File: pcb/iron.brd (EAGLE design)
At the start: 8 x 48 mm, 22 parts, among them IC1 AT24CS04-SOT23, IC2 TS507CLT, IC3 AD7995, IC4 ESDA6V1SC5, X1 LUMBERG_KLB_4

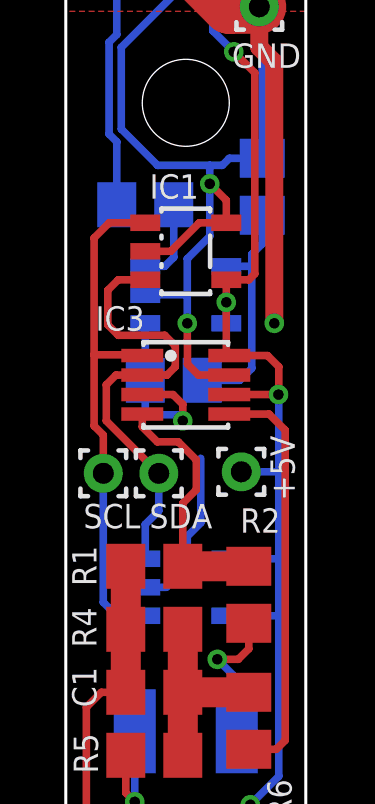
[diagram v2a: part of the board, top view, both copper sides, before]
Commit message: fixing op amp (iron,tweezer)
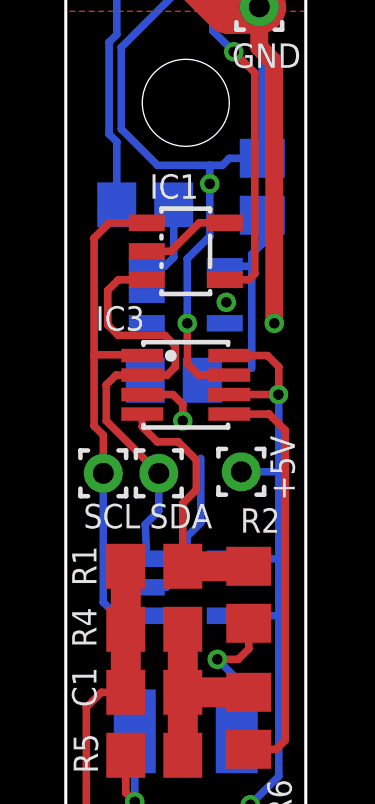
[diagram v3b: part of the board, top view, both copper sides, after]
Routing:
- net AD_TC: track 6.33 -> 2.03 mm
- net +5V: track 57.1 -> 53.9 mm
- net GND: track 60.1 -> 57.0 mm
- net FEEDBACK: track 7.91 -> 6.14 mm
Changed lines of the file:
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@@
 <attribute name="VALUE" x="3.585" y="21.49" size="1.27" layer="27" rot="R180"/>
 </element>
-<element name="R2" library="solderpi" library_urn="urn:adsk.eagle:library:1437534" package="R0805" package3d_urn="urn:adsk.eagle:package:1581953/2" value="68k @25°C, 1%, ß=4100 K" x="6.1" y="18" smashed="yes" rot="R90">
+<element name="R2" library="solderpi" library_urn="urn:adsk.eagle:library:1437534" package="R0805" package3d_urn="urn:adsk.eagle:package:1581953/4" value="68k @25°C, 1%, ß=4100 K" x="6.1" y="18" smashed="yes" rot="R90">
 <attribute name="NAME" x="5.815" y="20.07" size="0.8128" layer="25"/>
 <attribute name="VALUE" x="8.64" y="17.365" size="1.27" layer="27" rot="R90"/>
@@
 <attribute name="VALUE" x="9.09" y="32.235" size="1.27" layer="28" rot="MR270"/>
 </element>
-<element name="IC2" library="solderpi" library_urn="urn:adsk.eagle:library:1437534" package="SOT23-5L" package3d_urn="urn:adsk.eagle:package:1437676/4" value="TS507CLT" x="4" y="28" smashed="yes" rot="MR90">
+<element name="IC2" library="solderpi" library_urn="urn:adsk.eagle:library:1437534" package="SOT23-5L" package3d_urn="urn:adsk.eagle:package:1437676/7" value="TS507CLT" x="4" y="28" smashed="yes" rot="MR90">
 <attribute name="NAME" x="6.105" y="27.495" size="0.8128" layer="26" rot="MR90"/>
 <attribute name="OC_MOUSER" value="511-TS507CLT" x="4" y="28" size="1.778" layer="28" rot="MR90" display="off"/>
@@
 <attribute name="VALUE" x="5.85" y="22.7" size="0.0254" layer="27"/>
 </element>
-<element name="IC1" library="solderpi" library_urn="urn:adsk.eagle:library:1437534" package="SOT23-5L" package3d_urn="urn:adsk.eagle:package:1437676/4" value="AT24CS04-SOT23" x="4" y="29.45" smashed="yes" rot="R270">
+<element name="IC1" library="solderpi" library_urn="urn:adsk.eagle:library:1437534" package="SOT23-5L" package3d_urn="urn:adsk.eagle:package:1437676/7" value="AT24CS04-SOT23" x="4" y="29.45" smashed="yes" rot="R270">
 <attribute name="NAME" x="2.795" y="31.205" size="0.8128" layer="25"/>
 <attribute name="OC_MOUSER" value="556-AT24CS04-STUM-T" x="4" y="29.45" size="1.778" layer="27" rot="R270" display="off"/>
 <attribute name="VALUE" x="0.571" y="31.355" size="1.27" layer="27" rot="R270"/>
 </element>
-<element name="IC4" library="solderpi" library_urn="urn:adsk.eagle:library:1437534" package="SOT23-5L" package3d_urn="urn:adsk.eagle:package:1437676/4" value="ESDA6V1SC5" x="4" y="18.25" smashed="yes" rot="MR90">
+<element name="IC4" library="solderpi" library_urn="urn:adsk.eagle:library:1437534" package="SOT23-5L" package3d_urn="urn:adsk.eagle:package:1437676/7" value="ESDA6V1SC5" x="4" y="18.25" smashed="yes" rot="MR90">
 <attribute name="NAME" x="6.355" y="17.545" size="0.8128" layer="26" rot="MR90"/>
 <attribute name="VALUE" x="0.571" y="16.345" size="1.27" layer="28" rot="MR90"/>
@@
 <wire x1="4" y1="39.05" x2="4" y2="44.15" width="1.8" layer="1"/>
 <wire x1="5.45" y1="37.6" x2="4" y2="39.05" width="1.8" layer="1"/>
-<wire x1="5.35" y1="31.15" x2="4.8" y2="31.7" width="0.254" layer="1"/>
 <via x="4.8" y="31.7" extent="1-16" drill="0.35"/>
 <contactref element="IC1" pad="2"/>
 <contactref element="IC1" pad="5"/>
-<wire x1="5.35" y1="30.4" x2="5.35" y2="31.15" width="0.254" layer="1"/>
-<wire x1="2.65" y1="29.45" x2="3.5" y2="29.45" width="0.254" layer="1"/>
+<wire x1="2.7" y1="29.45" x2="3.5" y2="29.45" width="0.254" layer="1"/>
 <wire x1="3.5" y1="29.45" x2="4.45" y2="30.4" width="0.254" layer="1"/>
-<wire x1="4.45" y1="30.4" x2="5.35" y2="30.4" width="0.254" layer="1"/>
+<wire x1="4.45" y1="30.4" x2="5.3" y2="30.4" width="0.254" layer="1"/>
 <polygon width="0.2" layer="16" isolate="0.3048" rank="2">
 <vertex x="0" y="48"/>
@@
 <wire x1="5.7" y1="13.45" x2="5.7" y2="15.2" width="0.254" layer="16"/>
 <contactref element="IC4" pad="2"/>
-<wire x1="2.65" y1="18.25" x2="3.35" y2="18.25" width="0.254" layer="16"/>
+<wire x1="2.7" y1="18.25" x2="3.35" y2="18.25" width="0.254" layer="16"/>
 <wire x1="3.35" y1="18.25" x2="4.05" y2="18.95" width="0.254" layer="16"/>
 <wire x1="4.05" y1="18.95" x2="4.05" y2="19.95" width="0.254" layer="16"/>
@@
 <wire x1="6.45" y1="36.25" x2="6.45" y2="37.6" width="0.6" layer="1"/>
 <wire x1="6.95" y1="35.75" x2="6.45" y2="36.25" width="0.6" layer="1"/>
-<contactref element="IC2" pad="2"/>
 <wire x1="4.05" y1="27.05" x2="4.05" y2="28" width="0.254" layer="16"/>
 <wire x1="4.05" y1="28" x2="4.05" y2="29.2" width="0.254" layer="16"/>
 <wire x1="4.05" y1="29.2" x2="4.8" y2="29.95" width="0.254" layer="16"/>
-<wire x1="2.65" y1="28" x2="4.05" y2="28" width="0.254" layer="16"/>
+<contactref element="IC2" pad="2"/>
+<wire x1="4.8" y1="29.95" x2="4.45" y2="30.4" width="0" layer="19" extent="1-16"/>
 </signal>
 <signal name="AD_COMP">
@@
 <wire x1="7.1" y1="19.2" x2="7.1" y2="22.1" width="0.254" layer="16"/>
 <wire x1="7.1" y1="22.1" x2="7.1" y2="24.6642" width="0.254" layer="16"/>
-<wire x1="5.35" y1="19.2" x2="7.1" y2="19.2" width="0.254" layer="16"/>
+<wire x1="5.3" y1="19.2" x2="7.1" y2="19.2" width="0.254" layer="16"/>
 <wire x1="7.1" y1="11.95" x2="6.15" y2="11" width="0.254" layer="16"/>
 <via x="6.15" y="11" extent="1-16" drill="0.35"/>
@@
 <wire x1="1.1858" y1="14.75" x2="2" y2="14.75" width="0.254" layer="1"/>
 <wire x1="5.15" y1="10" x2="1.2858" y2="10" width="0.254" layer="1"/>
-<wire x1="5.35" y1="17.3" x2="7.1" y2="17.3" width="0.254" layer="16"/>
+<wire x1="5.3" y1="17.3" x2="7.1" y2="17.3" width="0.254" layer="16"/>
 <wire x1="5.85" y1="22.1" x2="7.1" y2="22.1" width="0.254" layer="16"/>
-<contactref element="IC2" pad="5"/>
-<wire x1="5.35" y1="27.05" x2="5.35" y2="27.75" width="0.254" layer="16"/>
 <via x="5.35" y="27.75" extent="1-16" drill="0.35"/>
-<wire x1="5.35" y1="27.75" x2="5.35" y2="28.5" width="0.254" layer="1"/>
-<wire x1="5.45" y1="25.975" x2="5.35" y2="25.975" width="0.254" layer="1"/>
-<wire x1="5.35" y1="25.975" x2="5.35" y2="27.75" width="0.254" layer="1"/>
-<wire x1="5.35" y1="28.5" x2="6.1" y2="28.5" width="0.254" layer="1"/>
+<wire x1="5.3" y1="28.5" x2="6.1" y2="28.5" width="0.254" layer="1"/>
 <wire x1="6.1" y1="28.5" x2="6.3" y2="28.7" width="0.254" layer="1"/>
 <wire x1="6.3" y1="28.7" x2="6.3" y2="35.4" width="0.254" layer="1"/>
@@
 <wire x1="5.6" y1="36.1" x2="4.9" y2="36.8" width="0.254" layer="16"/>
 <wire x1="4.9" y1="36.8" x2="4.9" y2="40.7" width="0.254" layer="16"/>
+<contactref element="IC2" pad="5"/>
+<wire x1="5.35" y1="27.75" x2="5.3" y2="27.05" width="0" layer="19" extent="16-16"/>
 </signal>
 <signal name="SCL">
@@
 <wire x1="2.525" y1="26" x2="0.9436" y2="26" width="0.254" layer="1"/>
 <contactref element="IC1" pad="1"/>
-<wire x1="2.65" y1="30.4" x2="1.45" y2="30.4" width="0.254" layer="1"/>
+<wire x1="2.7" y1="30.4" x2="1.45" y2="30.4" width="0.254" layer="1"/>
 <contactref element="IC4" pad="1"/>
-<wire x1="2.65" y1="17.3" x2="1.7" y2="17.3" width="0.254" layer="16"/>
+<wire x1="2.7" y1="17.3" x2="1.7" y2="17.3" width="0.254" layer="16"/>
 <wire x1="1.7" y1="17.3" x2="1.25" y2="17.75" width="0.254" layer="16"/>
 <wire x1="1.25" y1="17.75" x2="1.25" y2="22.05" width="0.254" layer="16"/>
@@
 <wire x1="1.4" y1="28.15" x2="1.75" y2="28.5" width="0.254" layer="1"/>
 <contactref element="IC1" pad="3"/>
-<wire x1="2.65" y1="28.5" x2="1.75" y2="28.5" width="0.254" layer="1"/>
+<wire x1="2.7" y1="28.5" x2="1.75" y2="28.5" width="0.254" layer="1"/>
 <contactref element="IC4" pad="3"/>
-<wire x1="2.65" y1="19.2" x2="2.65" y2="20.35" width="0.254" layer="16"/>
+<wire x1="2.7" y1="19.2" x2="2.65" y2="20.35" width="0.254" layer="16"/>
 <wire x1="3.1" y1="20.8" x2="3.1" y2="22.05" width="0.254" layer="16"/>
 <wire x1="2.65" y1="20.35" x2="3.1" y2="20.8" width="0.254" layer="16"/>
@@
 <contactref element="R8" pad="1"/>
 <contactref element="IC2" pad="4"/>
-<wire x1="4.55" y1="25.15" x2="5.8" y2="25.15" width="0.254" layer="16"/>
-<wire x1="5.8" y1="25.15" x2="6.2" y2="25.55" width="0.254" layer="16"/>
 <wire x1="6.2" y1="29.35" x2="6.55" y2="29.7" width="0.254" layer="16"/>
 <wire x1="6.55" y1="29.7" x2="6.55" y2="30.65" width="0.254" layer="16"/>
 <wire x1="6.2" y1="25.55" x2="6.2" y2="28.95" width="0.254" layer="16"/>
 <wire x1="6.2" y1="28.95" x2="6.2" y2="29.35" width="0.254" layer="16"/>
-<wire x1="5.35" y1="28.95" x2="6.2" y2="28.95" width="0.254" layer="16"/>
+<wire x1="5.3" y1="28.95" x2="6.2" y2="28.95" width="0.254" layer="16"/>
+<wire x1="4.55" y1="25.15" x2="6.2" y2="25.55" width="0" layer="19" extent="16-16"/>
 </signal>
 <signal name="AD_TC">
@@
 <contactref element="IC2" pad="1"/>
 <contactref element="IC3" pad="3"/>
-<wire x1="2.65" y1="27.05" x2="2.65" y2="25.15" width="0.254" layer="16"/>
 <wire x1="2.55" y1="24.675" x2="3.575" y2="24.675" width="0.254" layer="1"/>
 <wire x1="3.575" y1="24.675" x2="3.9" y2="24.35" width="0.254" layer="1"/>
 <wire x1="3.9" y1="24.35" x2="3.9" y2="23.8" width="0.254" layer="1"/>
 <via x="3.9" y="23.8" extent="1-16" drill="0.35"/>
-<wire x1="3.9" y1="23.8" x2="3.7" y2="24" width="0.254" layer="16"/>
-<wire x1="2.8" y1="24" x2="2.65" y2="24.15" width="0.254" layer="16"/>
-<wire x1="2.65" y1="24.15" x2="2.65" y2="25.15" width="0.254" layer="16"/>
-<wire x1="3.7" y1="24" x2="2.8" y2="24" width="0.254" layer="16"/>
+<wire x1="2.65" y1="25.15" x2="2.7" y2="27.05" width="0" layer="19" extent="16-16"/>
+<wire x1="2.55" y1="24.675" x2="2.65" y2="25.15" width="0" layer="19" extent="1-16"/>
 </signal>
 <signal name="THERMO_UNFIL">
@@
 <contactref element="R7" pad="1"/>
 <contactref element="IC2" pad="3"/>
-<wire x1="2.65" y1="28.95" x2="3.3" y2="28.95" width="0.254" layer="16"/>
+<wire x1="2.7" y1="28.95" x2="3.3" y2="28.95" width="0.254" layer="16"/>
 <wire x1="3.3" y1="28.95" x2="3.6" y2="29.25" width="0.254" layer="16"/>
 <wire x1="3.6" y1="29.25" x2="3.6" y2="31" width="0.254" layer="16"/>

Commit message: iron drills deleted
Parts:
- moved R9 22.8 mm to (6.60, 18.5), flipped to the top, turned to 270 degrees
- moved X1 21.0 mm to (4.00, 26.4), flipped to the bottom
- moved SCL 20.7 mm to (4.00, 1.50)
- moved SDA 20.6 mm to (1.30, 1.50)
- moved +5V 20.6 mm to (6.70, 1.50)
- moved C2 20.5 mm to (1.40, 18.4), flipped to the top, turned to 270 degrees
- moved IC1 19.7 mm to (3.95, 9.80), flipped to the bottom, turned to 90 degrees
- moved R10 19.6 mm to (1.40, 12.7), flipped to the top
- moved HEATER 18.8 mm to (1.70, 21.6)
- moved GND 16.0 mm to (6.40, 21.6)
- moved IC2 14.9 mm to (4.00, 13.1), flipped to the top, turned to 180 degrees
- moved R7 12.6 mm to (4.00, 18.4), flipped to the top, turned to 90 degrees
- moved IC4 12.6 mm to (4.00, 5.70)
- moved R8 11.8 mm to (6.60, 13.8), flipped to the top, turned to 90 degrees
- moved IC3 11.3 mm to (4.00, 13.7), flipped to the bottom, turned to 90 degrees
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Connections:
- net AD_MOTION: now also IC3.3; no longer IC3.5
- net AD_TC: now also IC3.5; no longer IC3.3
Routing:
- net +5V: track 53.9 -> 37.3 mm, vias 4 -> 2
- net GND: track 57.0 -> 51.4 mm, vias 4 -> 6
- net AD_COMP: track 8.62 -> 4.49 mm
- net AD_MOTION: track 13.8 -> 9.77 mm, vias 0 -> 1
- net MOTION_FIL: track 6.40 -> 9.67 mm
- net AD_TC: track 2.03 -> 5.12 mm
- net HEATER: track 5.85 -> 3.05 mm
- net SCL: track 17.5 -> 14.8 mm
- net THERMO_UNFIL: track 14.9 -> 12.4 mm
- net SDA: track 15.1 -> 16.5 mm
- net THERMO_FIL: track 2.77 -> 3.54 mm
- net MOTION_DIV: track 4.02 -> 3.36 mm, vias 1 -> 0
- removed copper zone on layer 1, net +5V
- removed copper zone on layer 1, net GND
- removed copper zone on layer 16, net GND
- removed copper zone on layer 16, net HEATER
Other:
- board size 8 x 48 mm -> 8 x 27 mm

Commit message: parts reworked
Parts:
- removed HEATER: (no value), solderpi:1,6/0,8
- added PWR: (no value), solderpi:1,6/0,8
- C1, C2: device rcl:C0805 -> common:C0603
- R1, R4, R5, R6, R7, R8, R9: device rcl:R0805 -> common:R0603
- R10: value 2k 0,1% -> 2k 0.1%; device rcl:R0805 -> common:R0603
- R2: value 68k @25°C, 1%, ß=4100 K -> 68k @25°C, 1%, ß=3985 K; device solderpi:R0805 -> common:R0603
- moved R5 3.67 mm to (5.45, 7.65)
- moved C2 3.64 mm to (4.00, 15.9)
- moved GND 3.10 mm to (6.30, 18.5)
- moved X1 3.00 mm to (4.00, 23.4)
- moved R7 2.93 mm to (2.65, 15.8)
- moved R9 2.88 mm to (5.35, 15.9)
- moved R1 2.14 mm to (5.60, 15.8), turned to 180 degrees
- moved R2 2.12 mm to (2.40, 15.8), turned to 180 degrees
- moved R3 1.36 mm to (2.15, 6.25)
- moved R10 1.26 mm to (1.55, 11.4)
- moved IC3 1.20 mm to (4.00, 12.5)
- moved IC1 1.10 mm to (4.00, 8.70)
- moved R8 1.06 mm to (6.45, 12.7)
- moved IC2 1.05 mm to (4.00, 12.0)
- moved IC4 0.90 mm to (4.00, 4.80)
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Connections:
- net HEATER: now also PWR.1; no longer HEATER.1
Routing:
- net GND: track 51.4 -> 42.6 mm, vias 6 -> 5
- net MOTION_FIL: track 9.67 -> 4.20 mm
- net THERMO_UNFIL: track 12.4 -> 9.59 mm
- net THERMO_FIL: track 3.54 -> 1.87 mm
- net SCL: track 14.8 -> 13.4 mm
- net SDA: track 16.5 -> 15.5 mm
- net MOTION_DIV: track 3.36 -> 2.45 mm
- net AD_MOTION: track 9.77 -> 9.13 mm
- added copper zone on layer 1, net GND
- added copper zone on layer 16, net GND
- added copper zone on layer 1, net HEATER
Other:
- board size 8 x 27 mm -> 8 x 24 mm
